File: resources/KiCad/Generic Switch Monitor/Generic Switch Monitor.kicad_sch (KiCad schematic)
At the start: 5 parts, among them SW1 Microswitch, U1 ESP8266-01s

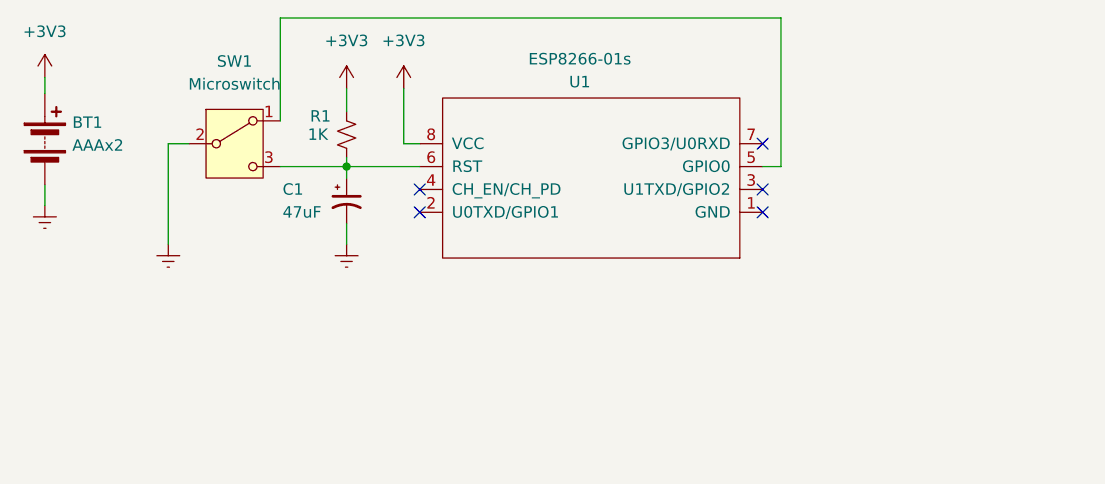
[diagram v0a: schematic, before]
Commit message: Changed reset circuit
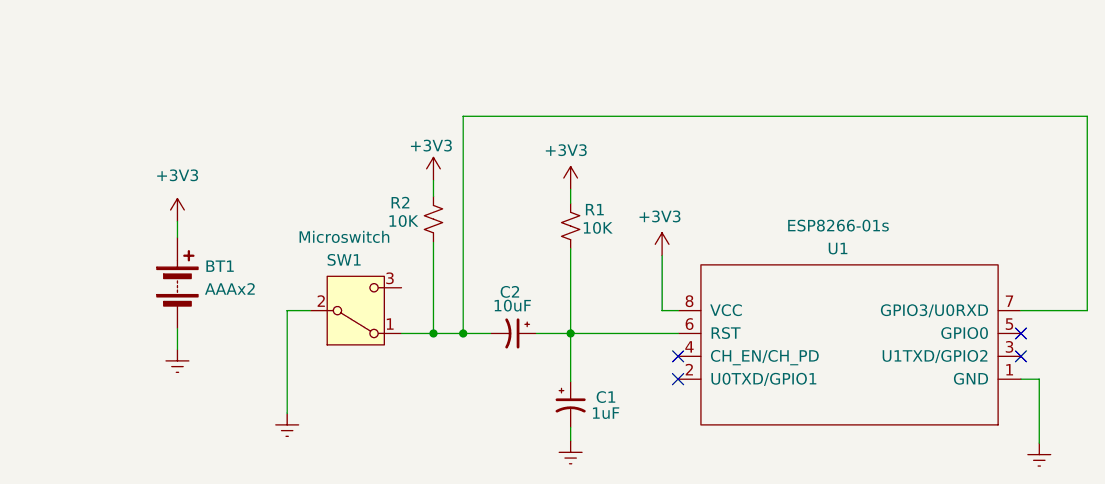
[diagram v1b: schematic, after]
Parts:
- added C2: 10uF, symbol Device:C_Polarized_Small_US
- added R2: 10K, symbol Device:R_Small_US
- C1: value 47uF -> 1uF
- R1: value 1K -> 10K
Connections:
- net +3V3: now also R2.1
- net Earth: now also U1.1 (GND)
- net at U1.5 (GPIO0): no longer SW1.1 (A)
- net at C1.1, R1.2, U1.6 (RST): now also C2.1; no longer SW1.3 (C)
- net at U1.7 (GPIO3/U0RXD): now also SW1.1 (A), C2.2, R2.2
- no-connect marks 5 -> 4
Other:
- company: (none) -> OmniTronics
- title: (none) -> Mousetrap Notifier using Generic Switch Monitor
- moved on the sheet: BT1, C1, R1, SW1, U1
